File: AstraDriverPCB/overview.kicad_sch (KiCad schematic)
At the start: 4 parts

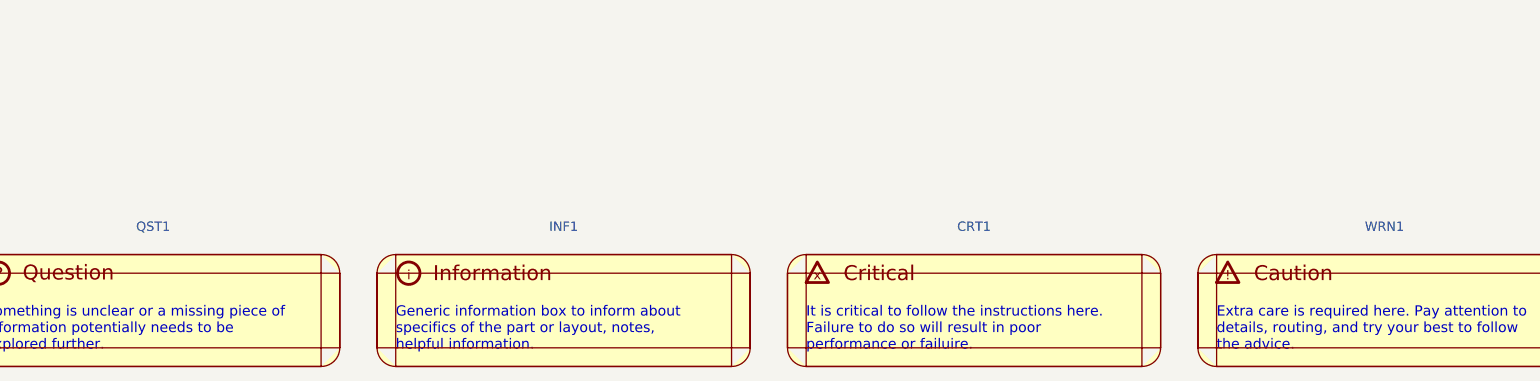
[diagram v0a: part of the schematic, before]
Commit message: Added all schematic components
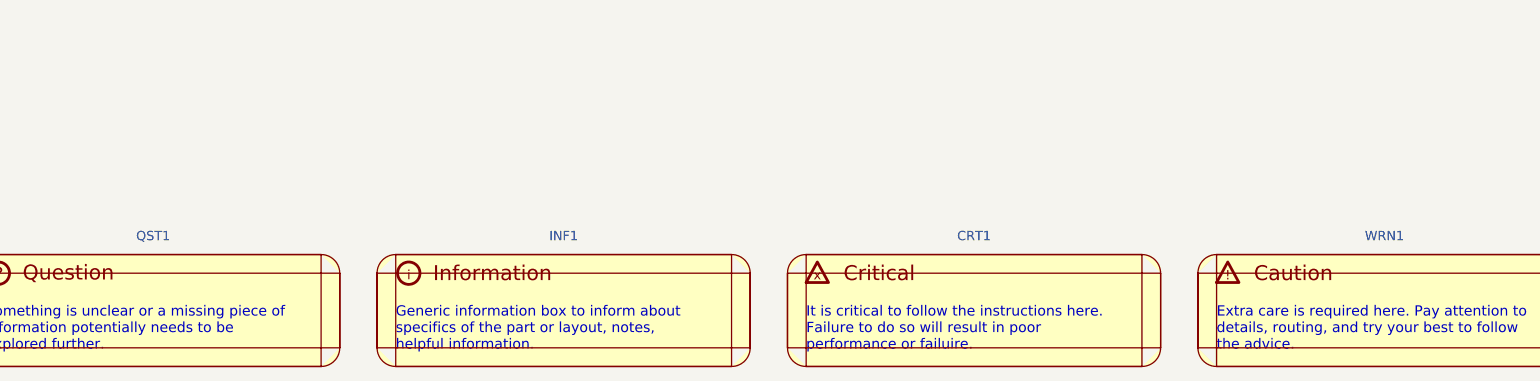
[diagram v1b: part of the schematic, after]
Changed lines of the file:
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@@
 		(fields_autoplaced yes)
 		(property "Reference" "INF1"
-			(at 101.6 158.75 0)
-			(effects
-				(font
-					(size 1.27 1.27)
-				)
-			)
-		)
-		(property "Value" "~"
-			(at 101.6 161.29 0)
-			(effects
-				(font
-					(size 1.27 1.27)
-				)
-			)
-		)
-		(property "Footprint" ""
-			(at 86.36 166.37 0)
-			(effects
-				(font
-					(size 1.27 1.27)
-				)
-				(hide yes)
-			)
-		)
-		(property "Datasheet" ""
-			(at 86.36 166.37 0)
-			(effects
-				(font
-					(size 1.27 1.27)
-				)
-				(hide yes)
-			)
-		)
-		(property "Description" ""
-			(at 86.36 166.37 0)
-			(effects
-				(font
-					(size 1.27 1.27)
-				)
-				(hide yes)
-			)
-		)
-		(instances
-			(project ""
-				(path "/9a751838-dce8-4d69-8a02-736625ac74e7/120c81b5-e37e-42ba-9ea8-918058b1f430"
+			(at 101.6 160.02 0)
+			(effects
+				(font
+					(size 1.27 1.27)
+				)
+			)
+		)
+		(property "Value" "~"
+			(at 86.36 166.37 0)
+			(effects
+				(font
+					(size 1.27 1.27)
+				)
+			)
+		)
+		(property "Footprint" ""
+			(at 86.36 166.37 0)
+			(effects
+				(font
+					(size 1.27 1.27)
+				)
+				(hide yes)
+			)
+		)
+		(property "Datasheet" ""
+			(at 86.36 166.37 0)
+			(effects
+				(font
+					(size 1.27 1.27)
+				)
+				(hide yes)
+			)
+		)
+		(property "Description" ""
+			(at 86.36 166.37 0)
+			(effects
+				(font
+					(size 1.27 1.27)
+				)
+				(hide yes)
+			)
+		)
+		(instances
+			(project ""
+				(path "/9a751838-dce8-4d69-8a02-736625ac74e7/120c81b5-e37e-42ba-9ea8-918058b1f430"
+					(reference "INF1")
+					(unit 1)
+				)
+			)
+			(project ""
+				(path "/d8760d88-6646-4dd8-a980-02e776803cc5/266764c8-9259-40c1-8d01-d8390298a222"
 					(reference "INF1")
 					(unit 1)
@@
 		(fields_autoplaced yes)
 		(property "Reference" "WRN1"
-			(at 213.36 158.75 0)
-			(effects
-				(font
-					(size 1.27 1.27)
-				)
-			)
-		)
-		(property "Value" "~"
-			(at 213.36 161.29 0)
-			(effects
-				(font
-					(size 1.27 1.27)
-				)
-			)
-		)
-		(property "Footprint" ""
-			(at 198.882 166.37 0)
-			(effects
-				(font
-					(size 1.27 1.27)
-				)
-				(hide yes)
-			)
-		)
-		(property "Datasheet" ""
-			(at 198.882 166.37 0)
-			(effects
-				(font
-					(size 1.27 1.27)
-				)
-				(hide yes)
-			)
-		)
-		(property "Description" ""
-			(at 198.882 166.37 0)
-			(effects
-				(font
-					(size 1.27 1.27)
-				)
-				(hide yes)
-			)
-		)
-		(instances
-			(project ""
-				(path "/9a751838-dce8-4d69-8a02-736625ac74e7/120c81b5-e37e-42ba-9ea8-918058b1f430"
+			(at 213.36 160.02 0)
+			(effects
+				(font
+					(size 1.27 1.27)
+				)
+			)
+		)
+		(property "Value" "~"
+			(at 198.882 166.37 0)
+			(effects
+				(font
+					(size 1.27 1.27)
+				)
+			)
+		)
+		(property "Footprint" ""
+			(at 198.882 166.37 0)
+			(effects
+				(font
+					(size 1.27 1.27)
+				)
+				(hide yes)
+			)
+		)
+		(property "Datasheet" ""
+			(at 198.882 166.37 0)
+			(effects
+				(font
+					(size 1.27 1.27)
+				)
+				(hide yes)
+			)
+		)
+		(property "Description" ""
+			(at 198.882 166.37 0)
+			(effects
+				(font
+					(size 1.27 1.27)
+				)
+				(hide yes)
+			)
+		)
+		(instances
+			(project ""
+				(path "/9a751838-dce8-4d69-8a02-736625ac74e7/120c81b5-e37e-42ba-9ea8-918058b1f430"
+					(reference "WRN1")
+					(unit 1)
+				)
+			)
+			(project ""
+				(path "/d8760d88-6646-4dd8-a980-02e776803cc5/266764c8-9259-40c1-8d01-d8390298a222"
 					(reference "WRN1")
 					(unit 1)
@@
 		(fields_autoplaced yes)
 		(property "Reference" "CRT1"
-			(at 157.48 158.75 0)
-			(effects
-				(font
-					(size 1.27 1.27)
-				)
-			)
-		)
-		(property "Value" "~"
-			(at 157.48 161.29 0)
-			(effects
-				(font
-					(size 1.27 1.27)
-				)
-			)
-		)
-		(property "Footprint" ""
-			(at 143.002 166.37 0)
-			(effects
-				(font
-					(size 1.27 1.27)
-				)
-				(hide yes)
-			)
-		)
-		(property "Datasheet" ""
-			(at 143.002 166.37 0)
-			(effects
-				(font
-					(size 1.27 1.27)
-				)
-				(hide yes)
-			)
-		)
-		(property "Description" ""
-			(at 143.002 166.37 0)
-			(effects
-				(font
-					(size 1.27 1.27)
-				)
-				(hide yes)
-			)
-		)
-		(instances
-			(project ""
-				(path "/9a751838-dce8-4d69-8a02-736625ac74e7/120c81b5-e37e-42ba-9ea8-918058b1f430"
+			(at 157.48 160.02 0)
+			(effects
+				(font
+					(size 1.27 1.27)
+				)
+			)
+		)
+		(property "Value" "~"
+			(at 143.002 166.37 0)
+			(effects
+				(font
+					(size 1.27 1.27)
+				)
+			)
+		)
+		(property "Footprint" ""
+			(at 143.002 166.37 0)
+			(effects
+				(font
+					(size 1.27 1.27)
+				)
+				(hide yes)
+			)
+		)
+		(property "Datasheet" ""
+			(at 143.002 166.37 0)
+			(effects
+				(font
+					(size 1.27 1.27)
+				)
+				(hide yes)
+			)
+		)
+		(property "Description" ""
+			(at 143.002 166.37 0)
+			(effects
+				(font
+					(size 1.27 1.27)
+				)
+				(hide yes)
+			)
+		)
+		(instances
+			(project ""
+				(path "/9a751838-dce8-4d69-8a02-736625ac74e7/120c81b5-e37e-42ba-9ea8-918058b1f430"
+					(reference "CRT1")
+					(unit 1)
+				)
+			)
+			(project ""
+				(path "/d8760d88-6646-4dd8-a980-02e776803cc5/266764c8-9259-40c1-8d01-d8390298a222"
 					(reference "CRT1")
 					(unit 1)
@@
 		(fields_autoplaced yes)
 		(property "Reference" "QST1"
-			(at 45.72 158.75 0)
-			(effects
-				(font
-					(size 1.27 1.27)
-				)
-			)
-		)
-		(property "Value" "~"
-			(at 45.72 161.29 0)
+			(at 45.72 160.02 0)
+			(effects
+				(font
+					(size 1.27 1.27)
+				)
+			)
+		)
+		(property "Value" "~"
+			(at 31.242 166.37 0)
 			(effects
 				(font
@@
 					(reference "QST1")
 					(unit 1)
+				)
+			)
+			(project ""
+				(path "/d8760d88-6646-4dd8-a980-02e776803cc5/266764c8-9259-40c1-8d01-d8390298a222"
+					(reference "QST1")
+					(unit 1)

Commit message: Prepare for review, cleanup
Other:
- note added: "Channel 1 Blue and CY"
- note added: "Channel 2 Blue and CY"
- note added: "Channel 3 Green"
- note added: "Channel 4 Red"
- note added: "The center of the board will have a 102x30mm copper heat sink attached to it."
- note removed: "10"
- note removed: "11"
- note removed: "12"
- note removed: "13"
- note removed: "14"
- note removed: "15"
- note removed: "16"
- note removed: "3.3V to 5V Logic Shifter"
- note removed: "5V GPIO Connectors"
- note removed: "5V Protection"
- note removed: "9"
- note removed: "Button, Status LED, UART, I2S"
- note removed: "Fan, Temperature, Screen I2C"
- note removed: "MCU"
- note removed: "MCU Enable and Boot"
- note removed: "PWM Connector"
- note removed: "Second time creating a PCB. Mistakes were probably made."
- note removed: "UART to RS-485"
- note removed: "USB-C"
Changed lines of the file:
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@@
-		)
-	)
-	(text "16"
-		(exclude_from_sim no)
-		(at 111.76 99.06 0)
-		(effects
-			(font
-				(face "ING Me")
-				(size 3 3)
-			)
-			(justify left)
 		)
 	)
@@
 		)
 	)
-	(text "PWM Connector"
-		(exclude_from_sim no)
-		(at 121.92 88.9 0)
-		(effects
-			(font
-				(face "ING Me")
-				(size 3 3)
-			)
-			(justify left)
-		)
-	)
 	(text "1"
 		(exclude_from_sim no)
@@
 		)
 	)
-	(text "Misc"
-		(exclude_from_sim no)
-		(at 121.92 99.06 0)
-		(effects
-			(font
-				(face "ING Me")
-				(size 3 3)
-			)
-			(justify left)
-		)
-	)
 	(text "2"
 		(exclude_from_sim no)
@@
 		)
 	)
-	(text "11"
-		(exclude_from_sim no)
-		(at 111.76 73.66 0)
-		(effects
-			(font
-				(face "ING Me")
-				(size 3 3)
-			)
-			(justify left)
-		)
-	)
-	(text "3.3V to 5V Logic Shifter"
-		(exclude_from_sim no)
-		(at 121.92 73.66 0)
-		(effects
-			(font
-				(face "ING Me")
-				(size 3 3)
-			)
-			(justify left)
-		)
-	)
-	(text "UART to RS-485"
-		(exclude_from_sim no)
-		(at 121.92 68.58 0)
-		(effects
-			(font
-				(face "ING Me")
-				(size 3 3)
-			)
-			(justify left)
-		)
-	)
-	(text "15"
-		(exclude_from_sim no)
-		(at 111.76 93.98 0)
-		(effects
-			(font
-				(face "ING Me")
-				(size 3 3)
-			)
-			(justify left)
-		)
-	)
-	(text "Fan, Temperature, Screen I2C"
-		(exclude_from_sim no)
-		(at 121.92 83.82 0)
-		(effects
-			(font
-				(face "ING Me")
-				(size 3 3)
-			)
-			(justify left)
-		)
-	)
-	(text "5V Protection"
+	(text "Channel 3 Green"
 		(exclude_from_sim no)
 		(at 38.1 88.9 0)
@@
 				(face "ING Me")
 				(size 1.397 1.397)
-			)
-			(justify left)
-		)
-	)
-	(text "Page"
-		(exclude_from_sim no)
-		(at 101.6 50.8 0)
-		(effects
-			(font
-				(face "ING Me")
-				(size 4 4)
-			)
-			(justify left)
-		)
-	)
-	(text "12"
-		(exclude_from_sim no)
-		(at 111.76 78.74 0)
-		(effects
-			(font
-				(face "ING Me")
-				(size 3 3)
-			)
-			(justify left)
-		)
-	)
-	(text "13"
-		(exclude_from_sim no)
-		(at 111.76 83.82 0)
-		(effects
-			(font
-				(face "ING Me")
-				(size 3 3)
 			)
 			(justify left)
@@
 		)
 	)
-	(text "MCU Enable and Boot"
+	(text "Channel 2 Blue and CY"
 		(exclude_from_sim no)
 		(at 38.1 83.82 0)
@@
 		)
 	)
-	(text "MCU Enable and Boot"
+	(text "Misc"
 		(exclude_from_sim no)
 		(at 38.1 99.06 0)
@@
 		)
 	)
-	(text "5V GPIO Connectors"
-		(exclude_from_sim no)
-		(at 121.92 78.74 0)
-		(effects
-			(font
-				(face "ING Me")
-				(size 3 3)
-			)
-			(justify left)
-		)
-	)
 	(text "It is critical to follow the instructions here. \nFailure to do so will result in poor\nperformance or failuire."
 		(exclude_from_sim no)
@@
 				(face "ING Me")
 				(size 1.397 1.397)
-			)
-			(justify left)
-		)
-	)
-	(text "14"
-		(exclude_from_sim no)
-		(at 111.76 88.9 0)
-		(effects
-			(font
-				(face "ING Me")
-				(size 3 3)
 			)
 			(justify left)
@@
 		)
 	)
-	(text "MCU"
+	(text "Channel 4 Red"
 		(exclude_from_sim no)
 		(at 38.1 93.98 0)
@@
 		)
 	)
-	(text "Second time creating a PCB. Mistakes were probably made."
+	(text "The center of the board will have a 102x30mm copper heat sink attached to it."
 		(exclude_from_sim no)
 		(at 25.4 123.19 0)
@@
 		)
 	)
-	(text "10"
-		(exclude_from_sim no)
-		(at 111.76 68.58 0)
-		(effects
-			(font
-				(face "ING Me")
-				(size 3 3)
-			)
-			(justify left)
-		)
-	)
 	(text "4"
 		(exclude_from_sim no)
@@
 		)
 	)
-	(text "Description"
-		(exclude_from_sim no)
-		(at 120.65 50.8 0)
-		(effects
-			(font
-				(face "ING Me")
-				(size 4 4)
-			)
-			(justify left)
-		)
-	)
-	(text "9"
-		(exclude_from_sim no)
-		(at 111.76 63.5 0)
-		(effects
-			(font
-				(face "ING Me")
-				(size 3 3)
-			)
-			(justify left)
-		)
-	)
-	(text "MCU"
+	(text "Channel 1 Blue and CY"
 		(exclude_from_sim no)
 		(at 38.1 78.74 0)
 		(effects
 			(font
-				(face "ING Me")
-				(size 3 3)
-			)
-			(justify left)
-		)
-	)
-	(text "Button, Status LED, UART, I2S"
-		(exclude_from_sim no)
-		(at 121.92 93.98 0)
-		(effects
-			(font
-				(face "ING Me")
-				(size 3 3)
-			)
-			(justify left)
-		)
-	)
-	(text "USB-C"
-		(exclude_from_sim no)
-		(at 121.92 63.5 0)
-		(effects
-			(font

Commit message: Tweaks for JLC
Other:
- note added: "The center of the board will have a 102x30mm heat sink pad."
- note removed: "The center of the board will have a 102x30mm copper heat sink attached to it."
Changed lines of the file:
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@@
 		)
 	)
-	(text "The center of the board will have a 102x30mm copper heat sink attached to it."
+	(text "The center of the board will have a 102x30mm heat sink pad."
 		(exclude_from_sim no)
 		(at 25.4 123.19 0)

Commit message: Cleanup
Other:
- note added: "Test plugs will be hand-soldered on a single test board."
- note added: "Vias will be plugged and capped to avoid issues with exposed pads."
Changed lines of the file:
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@@
+		)
+	)
+	(text "Vias will be plugged and capped to avoid issues with exposed pads."
+		(exclude_from_sim no)
+		(at 25.4 129.54 0)
+		(effects
+			(font
+				(face "ING Me")
+				(size 3 3)
+			)
+			(justify left)
 		)
 	)
@@
 			)
 			(justify left)
+		)
+	)
+	(text "Test plugs will be hand-soldered on a single test board."
+		(exclude_from_sim no)
+		(at 25.4 135.89 0)
+		(effects
+			(font
+				(face "ING Me")
+				(size 3 3)
+			)
+			(justify left)
